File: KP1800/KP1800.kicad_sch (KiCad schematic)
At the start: 7 parts, among them U1 ATmega32U4-A

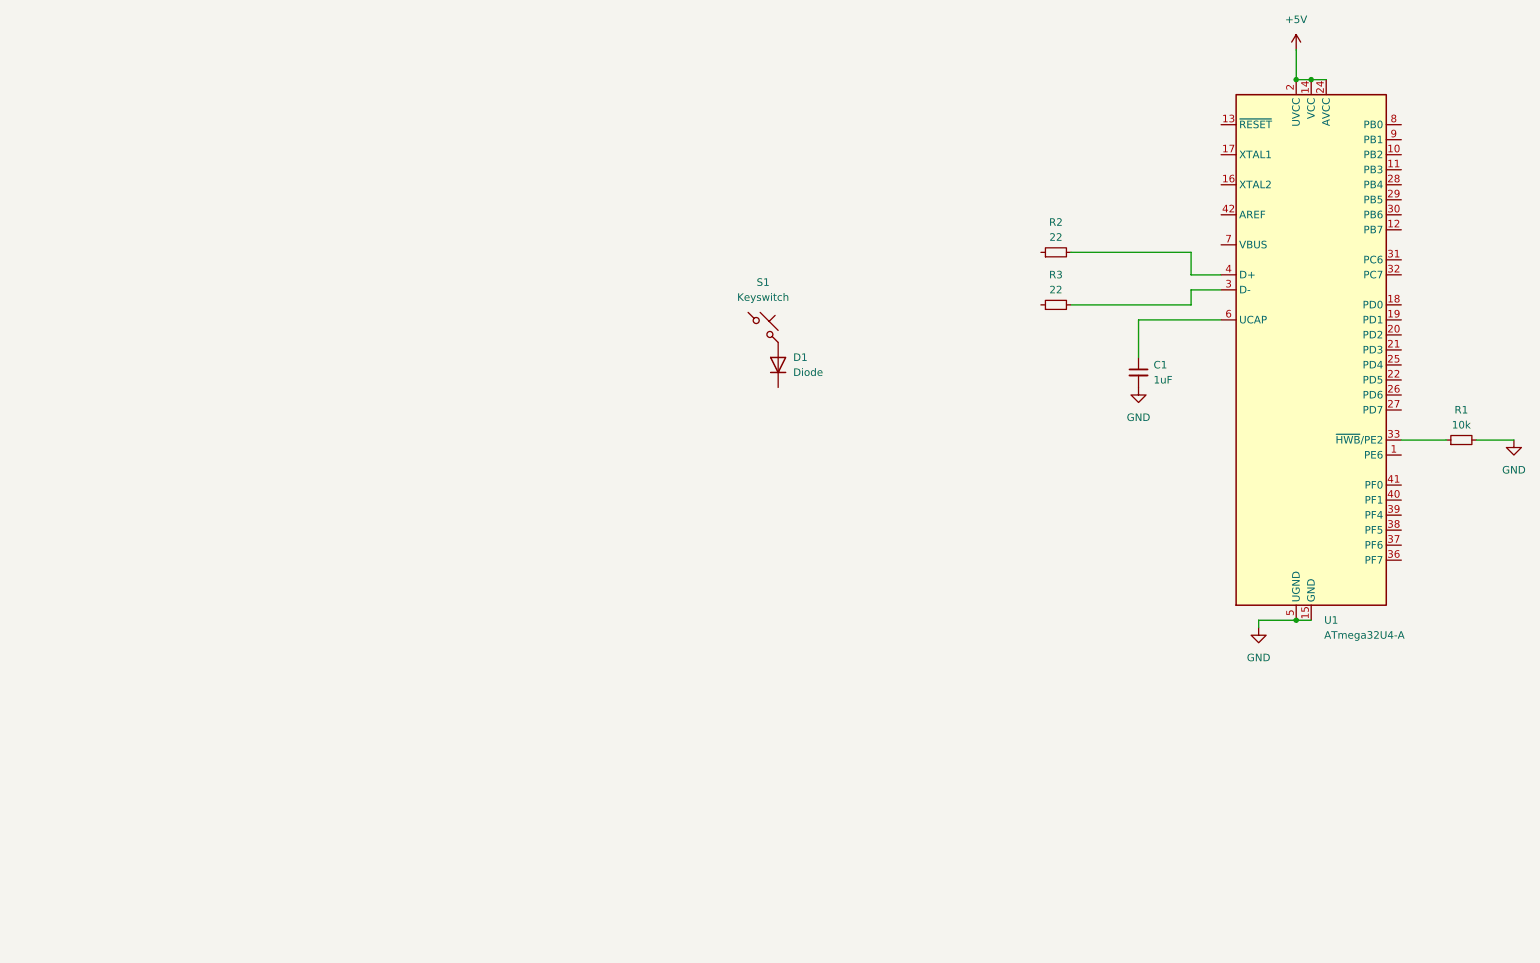
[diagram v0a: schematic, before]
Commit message: Completed MCU Circuit and USB Circuit
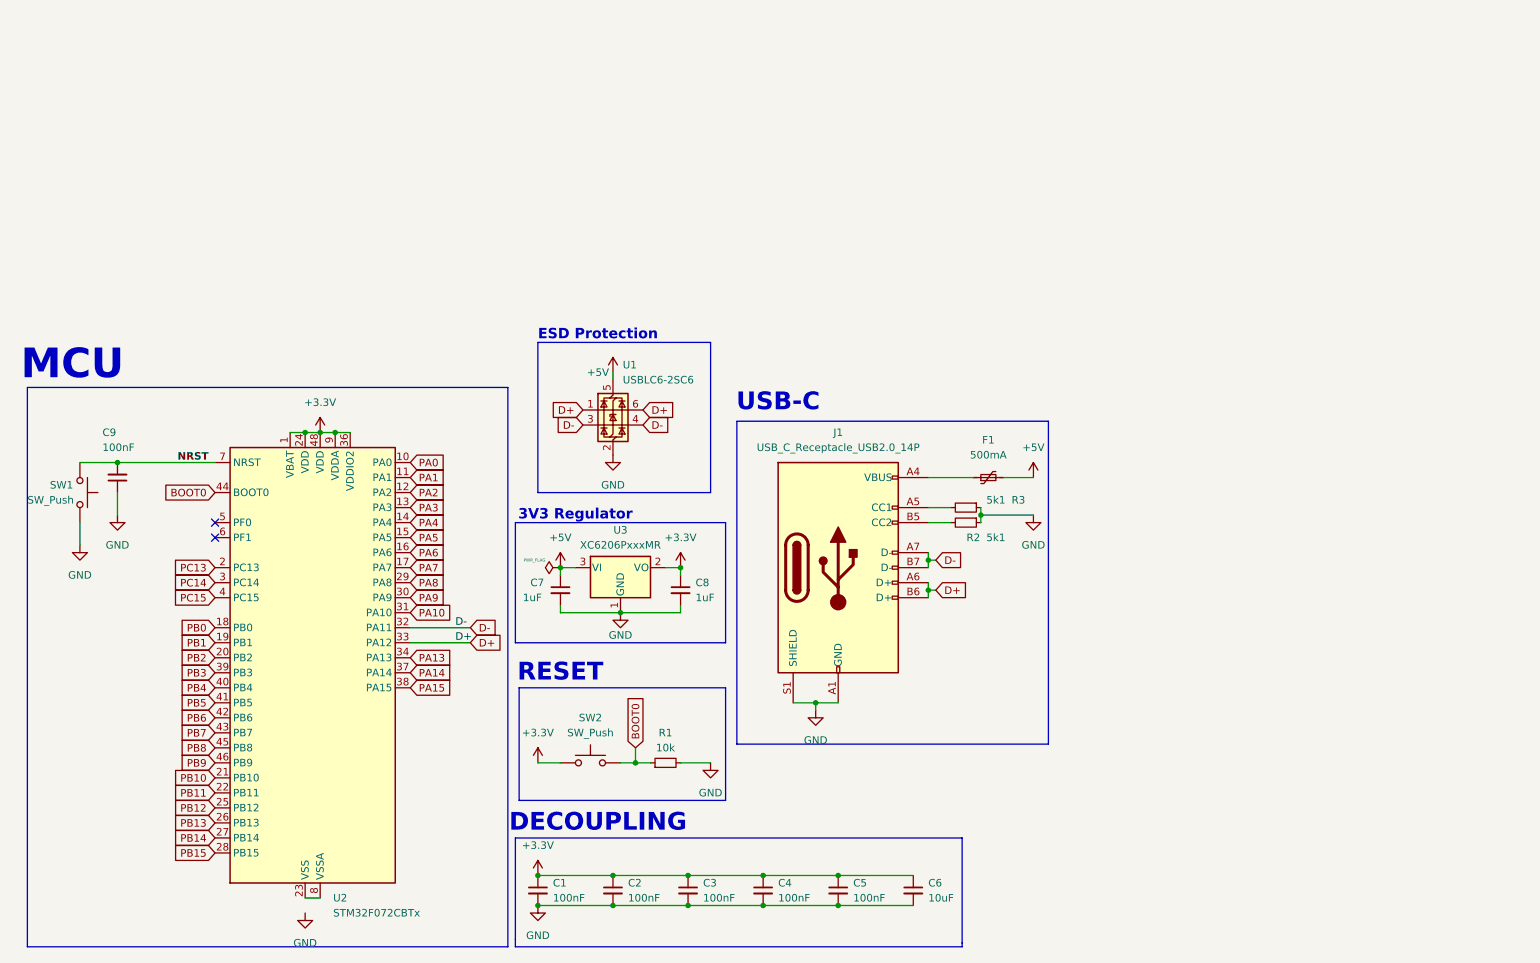
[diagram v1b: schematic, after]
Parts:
- removed D1: Diode, symbol ScottoKeebs:Placeholder_Diode
- removed S1: Keyswitch, symbol ScottoKeebs:Placeholder_Keyswitch
- removed U1: ATmega32U4-A, Package_QFP:TQFP-44_10x10mm_P0.8mm, symbol MCU_Microchip_ATmega:ATmega32U4-A
- added C2, C3, C4, C5, C9: 100nF, symbol Device:C_Small
- added C6: 10uF, symbol Device:C_Small
- added C7, C8: 1uF, symbol Device:C_Small
- added F1: 500mA, symbol Device:Polyfuse_Small
- added J1: USB_C_Receptacle_USB2.0_14P, symbol Connector:USB_C_Receptacle_USB2.0_14P
- added SW1, SW2: SW_Push, symbol Switch:SW_Push
- added U1: USBLC6-2SC6, Package_TO_SOT_SMD:SOT-23-6, symbol Power_Protection:USBLC6-2SC6
- added U2: STM32F072CBTx, Package_QFP:LQFP-48_7x7mm_P0.5mm, symbol MCU_ST_STM32F0:STM32F072CBTx
- added U3: XC6206PxxxMR, Package_TO_SOT_SMD:SOT-23-3, symbol Regulator_Linear:XC6206PxxxMR
- C1: value 1uF -> 100nF
- R2, R3: value 22 -> 5k1
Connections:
- net +5V: now also C7.1, F1.2, U1.5 (VBUS), U3.3 (VI)
- net GND: now also R2.1, R3.1, C2.2, C3.2, C4.2, C5.2, C6.2, C7.2, C8.2, C9.1, J1.A1 (GND), J1.A12 (GND), J1.B1 (GND), J1.B12 (GND), J1.S1 (SHIELD), SW1.2, U1.2 (GND), U3.1 (GND)
- net +3.3V: now reaches C1.1
- net +3.3V: now also C2.1, C3.1, C4.1, C5.1, C6.1, C8.1, SW2.1, U2.1 (VBAT), U2.24 (VDD), U2.36 (VDDIO2), U2.48 (VDD), U2.9 (VDDA), U3.2 (VO)
- net at R2.2: now also J1.B5 (CC2)
- net at R3.2: now also J1.A5 (CC1)
- net BOOT0: now reaches R1.1
- net BOOT0: now also SW2.2, U2.44 (BOOT0)
- new net: F1.1, J1.A4 (VBUS), J1.A9 (VBUS), J1.B4 (VBUS), J1.B9 (VBUS)
- new net: U2.23 (VSS), U2.35 (VSS), U2.47 (VSS), U2.8 (VSSA)
- new net D+: J1.A6 (D+), J1.B6 (D+), U1.1 (I/O1), U1.6 (I/O1), U2.33 (PA12)
- new net D-: J1.A7 (D-), J1.B7 (D-), U1.3 (I/O2), U1.4 (I/O2), U2.32 (PA11)
- new net NRST: C9.2, SW1.1, U2.7 (NRST)
- new net PA0: U2.10 (PA0)
- new net PA1: U2.11 (PA1)
- new net PA10: U2.31 (PA10)
- new net PA13: U2.34 (PA13)
- new net PA14: U2.37 (PA14)
- new net PA15: U2.38 (PA15)
- new net PA2: U2.12 (PA2)
- new net PA3: U2.13 (PA3)
- new net PA4: U2.14 (PA4)
- new net PA5: U2.15 (PA5)
- new net PA6: U2.16 (PA6)
- new net PA7: U2.17 (PA7)
- new net PA8: U2.29 (PA8)
- new net PA9: U2.30 (PA9)
- new net PB0: U2.18 (PB0)
- new net PB1: U2.19 (PB1)
- new net PB10: U2.21 (PB10)
- new net PB11: U2.22 (PB11)
- new net PB12: U2.25 (PB12)
- new net PB13: U2.26 (PB13)
- new net PB14: U2.27 (PB14)
- new net PB15: U2.28 (PB15)
- new net PB2: U2.20 (PB2)
- new net PB3: U2.39 (PB3)
- new net PB4: U2.40 (PB4)
- new net PB5: U2.41 (PB5)
- new net PB6: U2.42 (PB6)
- new net PB7: U2.43 (PB7)
- new net PB8: U2.45 (PB8)
- new net PB9: U2.46 (PB9)
- new net PC13: U2.2 (PC13)
- new net PC14: U2.3 (PC14)
- new net PC15: U2.4 (PC15)
- no-connect marks 0 -> 2
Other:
- note added: "3V3 Regulator"
- note added: "DECOUPLING"
- note added: "ESD Protection"
- note added: "MCU"
- note added: "RESET"
- note added: "USB-C"

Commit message: Formatted Matrix
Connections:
- net GND: now also U2.23 (VSS), U2.35 (VSS), U2.47 (VSS), U2.8 (VSSA)
- net VBUS: now reaches F1.1, J1.A4 (VBUS), J1.A9 (VBUS), J1.B4 (VBUS), J1.B9 (VBUS)
- net PA0 renamed A0
- net PA1 renamed A1
- net PA10: no longer names the net of U2.31 (PA10)
- net PA13: no longer names the net of U2.34 (PA13)
- net PA14 renamed A14
- net PA15 renamed A15
- net PA2 renamed A2
- net PA3 renamed A3
- net PA4 renamed A4
- net PA5 renamed A5
- net PA6 renamed A6
- net PA7: no longer names the net of U2.17 (PA7)
- net PA8: no longer names the net of U2.29 (PA8)
- net PA9: no longer names the net of U2.30 (PA9)
- net PB0 renamed B0
- net PB1 renamed B1
- net PB10 renamed B10
- net PB11 renamed B11
- net PB12 renamed B12
- net PB13 renamed B13
- net PB14 renamed B14
- net PB15 renamed B15
- net PB2 renamed B2
- net PB3 renamed B3
- net PB4 renamed B4
- net PB5 renamed B5
- net PB6 renamed B6
- net PB7 renamed B7
- net PB8 renamed B8
- net PB9 renamed B9
- net PC13: no longer names the net of U2.2 (PC13)
- net PC14: no longer names the net of U2.3 (PC14)
- net PC15: no longer names the net of U2.4 (PC15)
- no-connect marks 2 -> 10
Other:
- added sheet Matrix (matrix.kicad_sch)
- title: (none) -> KP1800 Keyboard PCB
- moved on the sheet: C1, C2, C3, C4, C5, C6, C7, C8, C9, F1, J1, R1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
